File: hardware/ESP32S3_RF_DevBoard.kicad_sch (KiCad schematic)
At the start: 25 parts, among them J1 USB4105-GF-A, J2 Conn_01x22, J3 Conn_01x22, SW1 BOOT, SW2 RESET, U1 ESD122DMYR, U2 LD1117DT33CTR, U3 ESP32-S3-WROOM-1-N8

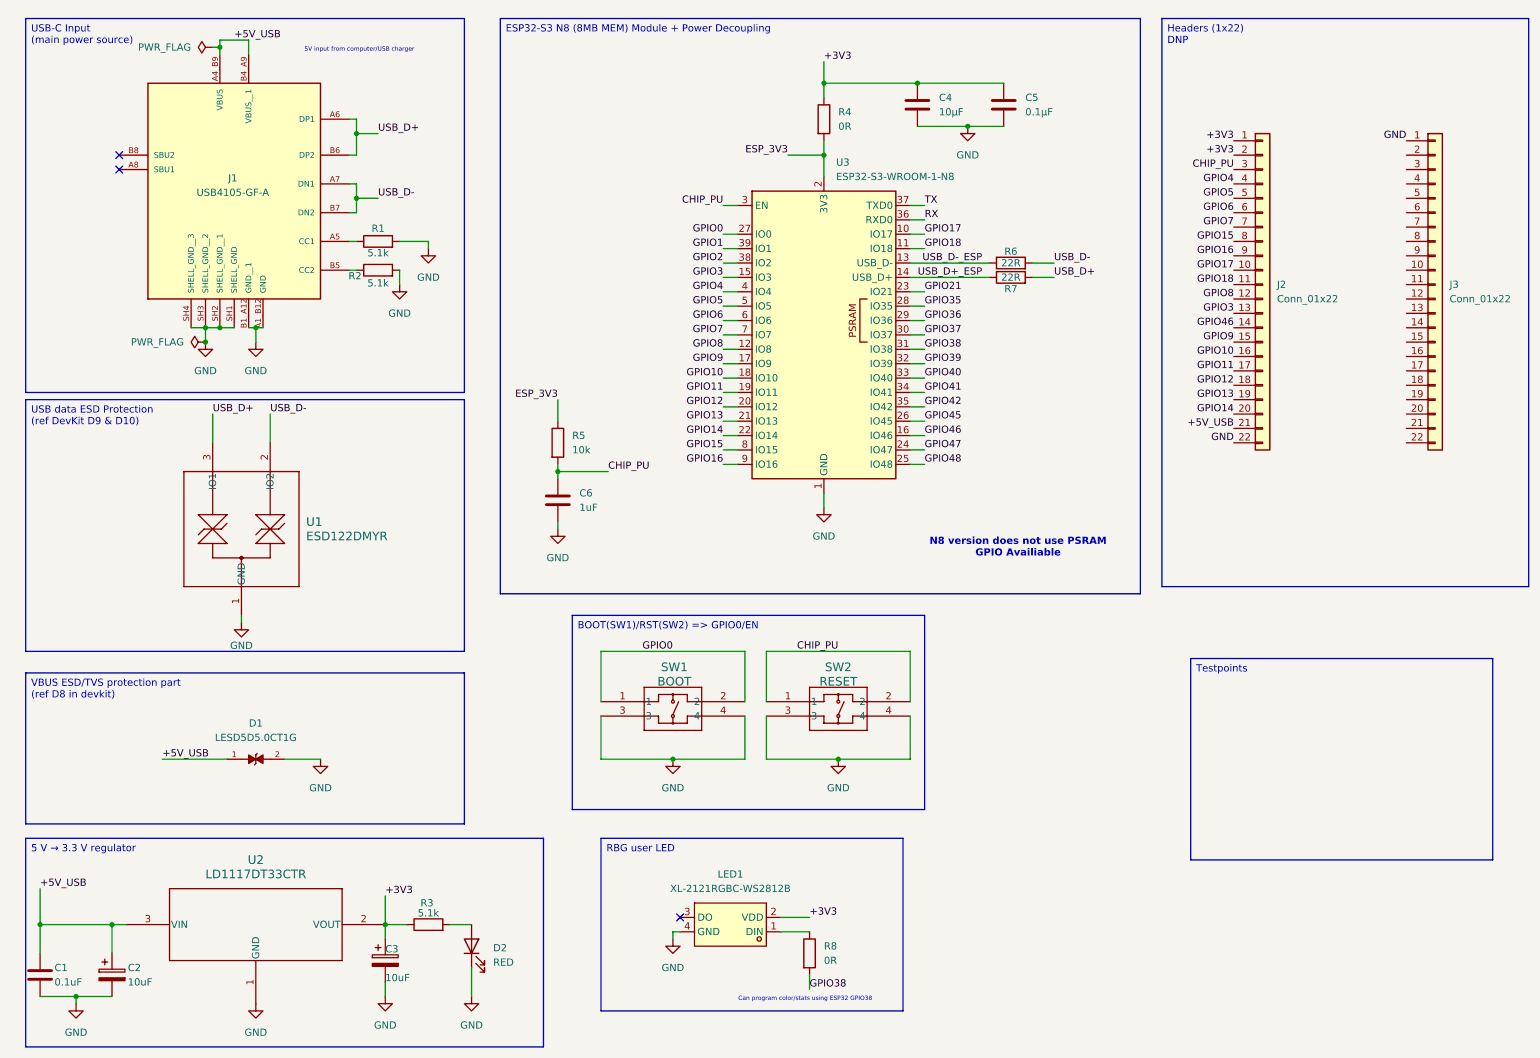
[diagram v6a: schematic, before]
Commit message: working on adding a level buffer 3.3v to 5v for the RGB
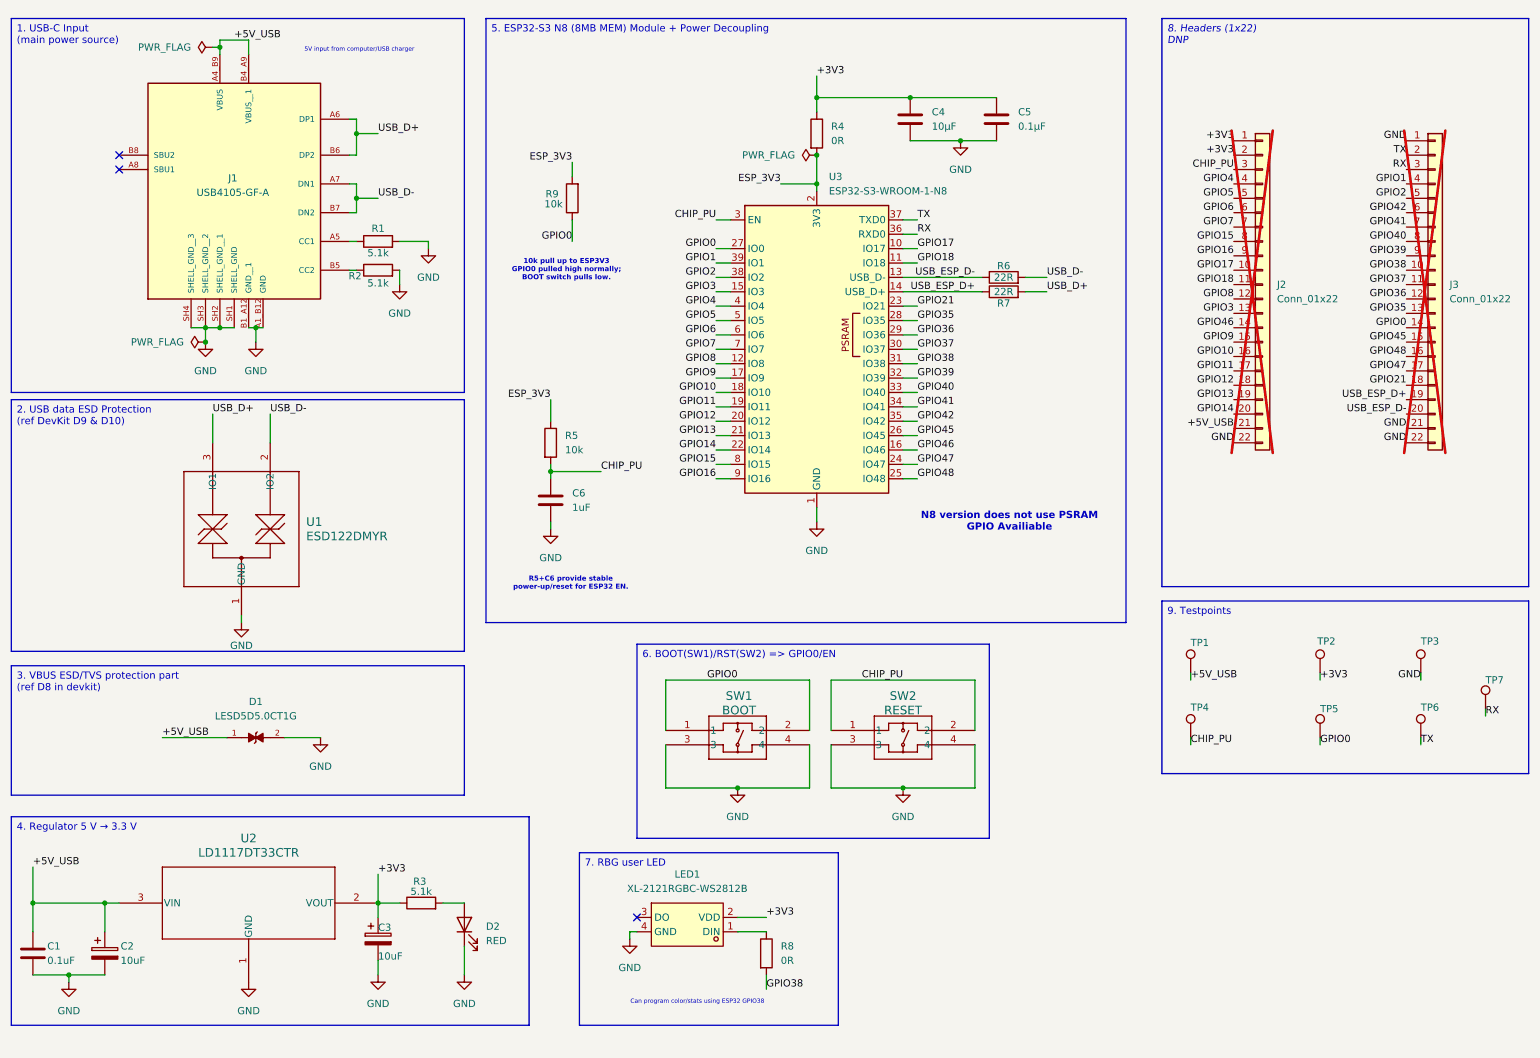
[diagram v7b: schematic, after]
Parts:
- added R9: 10k, Resistor_SMD:R_0603_1608Metric, symbol Device:R
- added TP1, TP2, TP3, TP4, TP5, TP6, TP7: TestPoint, TestPoint:TestPoint_Pad_D1.0mm, symbol Connector:TestPoint
- J2, J3: now not fitted
- R1, R2: footprint (none) -> Resistor_SMD:R_0603_1608Metric; JLCPCB/LCSC (none) -> C14677
- R5: footprint Resistor_SMD:R_0805_2012Metric -> Resistor_SMD:R_0603_1608Metric; LCSC/JLCPCB C17414 -> C25804; MPN 0805W8F1002T5E -> 0603WAF1002T5E; Power 125mW -> (none); Tolerance ±1% -> (none)
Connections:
- net USB_D+_ESP is gone; now on net USB_ESP_D+: R7.1, U3.14 (USB_D+)
- net USB_D-_ESP is gone; now on net USB_ESP_D-: R6.1, U3.13 (USB_D-)
- net +3V3: now also TP2.1
- net +5V_USB: now also TP1.1
- net CHIP_PU: now also TP4.1
- net ESP_3V3: now also R9.2
- net GND: now also J3.21 (Pin_21), J3.22 (Pin_22), TP3.1
- net GPIO0: now also J3.14 (Pin_14), R9.1, TP5.1
- net GPIO1: now also J3.4 (Pin_4)
- net GPIO2: now also J3.5 (Pin_5)
- net GPIO21: now also J3.18 (Pin_18)
- net GPIO35: now also J3.13 (Pin_13)
- net GPIO36: now also J3.12 (Pin_12)
- net GPIO37: now also J3.11 (Pin_11)
- net GPIO38: now also J3.10 (Pin_10)
- net GPIO39: now also J3.9 (Pin_9)
- net GPIO40: now also J3.8 (Pin_8)
- net GPIO41: now also J3.7 (Pin_7)
- net GPIO42: now also J3.6 (Pin_6)
- net GPIO45: now also J3.15 (Pin_15)
- net GPIO47: now also J3.17 (Pin_17)
- net GPIO48: now also J3.16 (Pin_16)
- net RX: now also J3.3 (Pin_3), TP7.1
- net TX: now also J3.2 (Pin_2), TP6.1
- net USB_ESP_D+: now reaches J3.19 (Pin_19)
- net USB_ESP_D-: now reaches J3.20 (Pin_20)
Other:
- note added: "10k pull up to ESP3V3 GPIO0 pulled high normally; BOOT switch pulls low."
- note added: "R5+C6 provide stable power-up/reset for ESP32 EN."
- moved on the sheet: C1, C2, C3, C4, C5, C6, D1, D2, LED1, R3, R4, R5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
